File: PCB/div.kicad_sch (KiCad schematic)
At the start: 26 parts

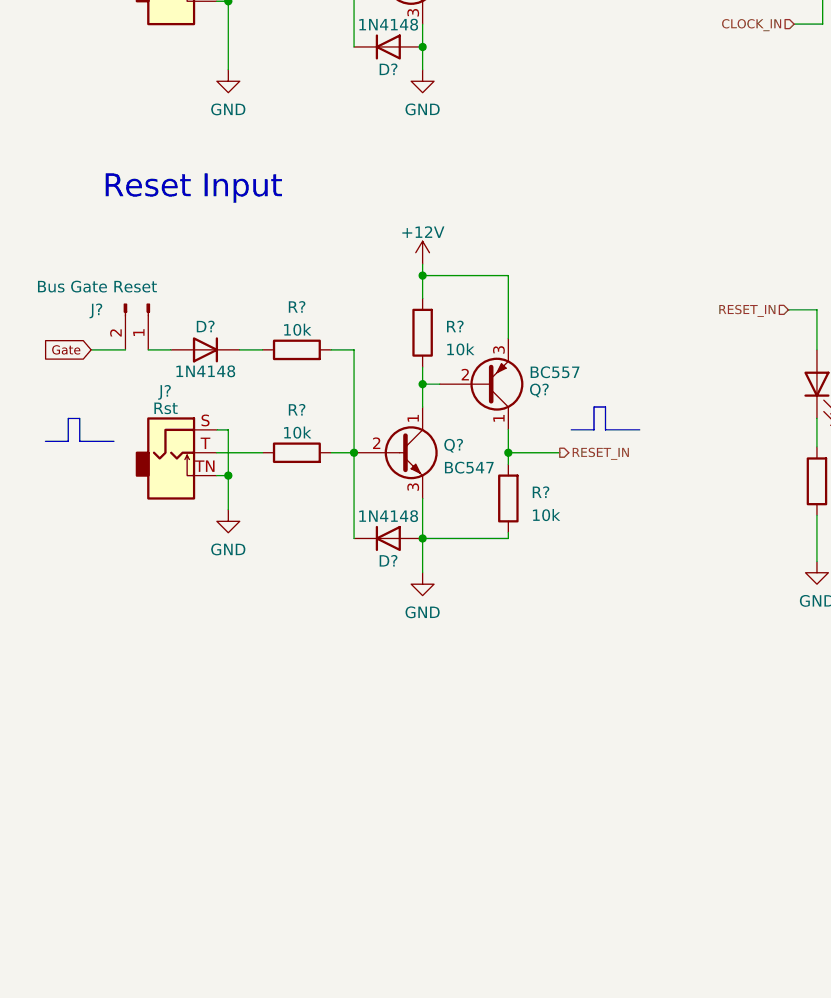
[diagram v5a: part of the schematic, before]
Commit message: :art: Add separate transistor stage for the bus reset input
This resolves the problems of backdriving and unwanted resistor
dividers between jack and bus input.
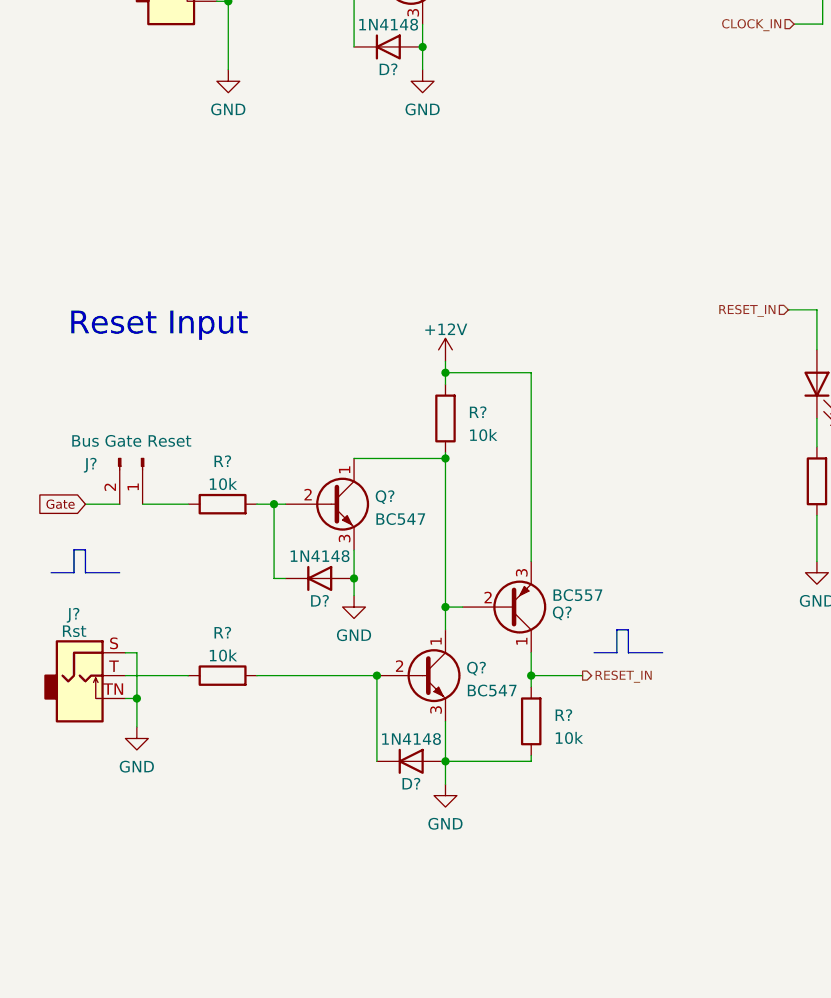
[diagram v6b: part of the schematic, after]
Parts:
- added Q?: BC547, Package_TO_SOT_THT:TO-92_Inline, symbol Transistor_BJT:BC547
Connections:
- net GND: now also D?.2 (A), Q?.3 (E)
- net at Q?.1 (C), Q?.2 (B), R?.1: now also Q?.1 (C)
- net at D?.1 (K): now also R?.2, Q?.2 (B); no longer R?.1
- net at J?.1 (Pin_1): now also R?.1; no longer D?.2 (A)
- net at D?.1 (K), Q?.2 (B), R?.2: no longer R?.2
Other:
- moved on the sheet: D?, J?, Q?, R?

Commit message: :pencil2: Fix naming of ferrite bead footprint
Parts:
- FB?: footprint mopsy:FBeadL4D4 -> moPsy:FBeadL4D4
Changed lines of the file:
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@@
       (effects (font (size 1.27 1.27)))
     )
-    (property "Footprint" "mopsy:FBeadL4D4" (at 83.82 180.848 90)
+    (property "Footprint" "moPsy:FBeadL4D4" (at 83.82 180.848 90)
       (effects (font (size 1.27 1.27)) hide)
     )

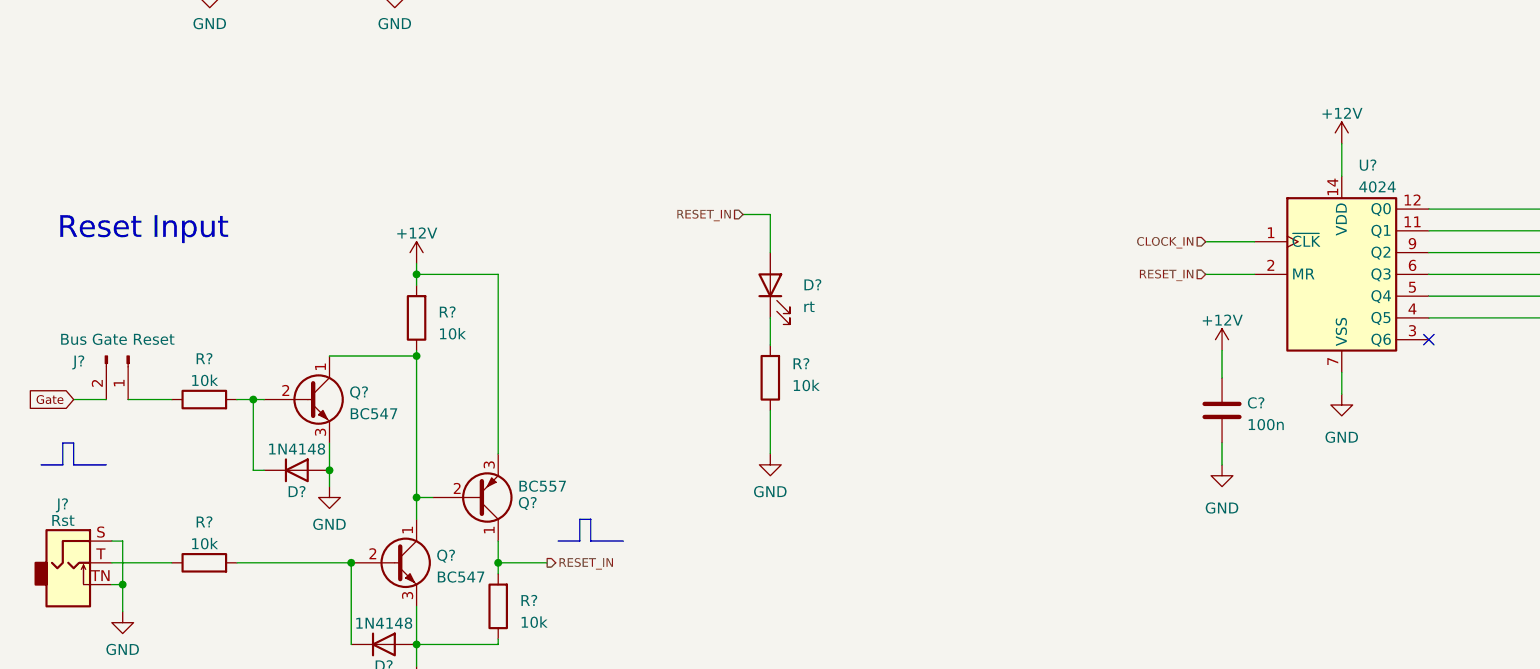
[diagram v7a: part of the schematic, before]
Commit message: :sparkles: Add symbol annotations
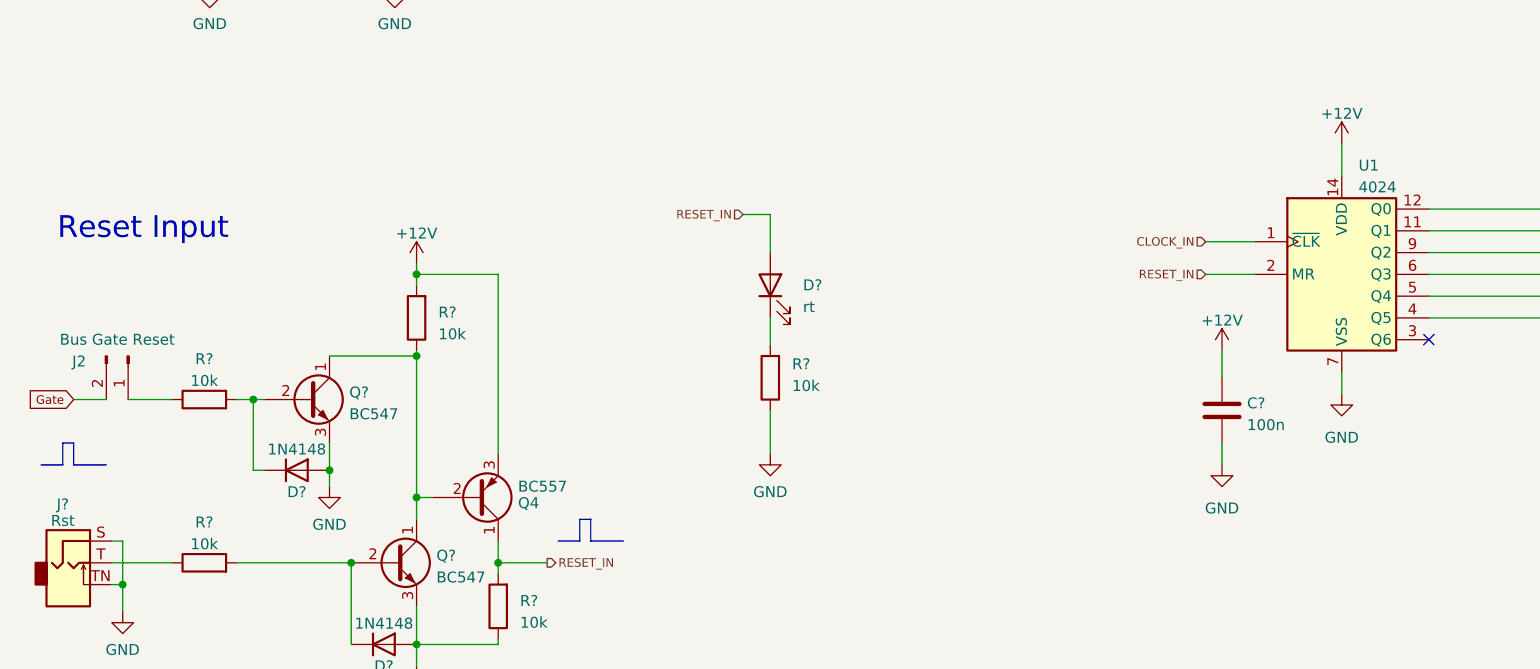
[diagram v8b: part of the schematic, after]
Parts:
- gave numbers to parts that had none: 3
